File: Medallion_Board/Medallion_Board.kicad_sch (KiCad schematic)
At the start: 80 parts, among them IC1 Wio-SX1262, J1 SWD HEADER, J2 EXPANSION, P1 JST_BTN_1, P2 JST_BTN_2, P3 JST_BTN_3, Q1 DMG3415U, U1 MDBT50Q-1MV2, U2 MAX17048G_T10, U3 LC86LICMD, U4 RT9080-33GJ5, U5 MCP73831T-2ACI_OT, U6 BNO085, X1 USB4085-GF-A, Y1 32.768KHZ

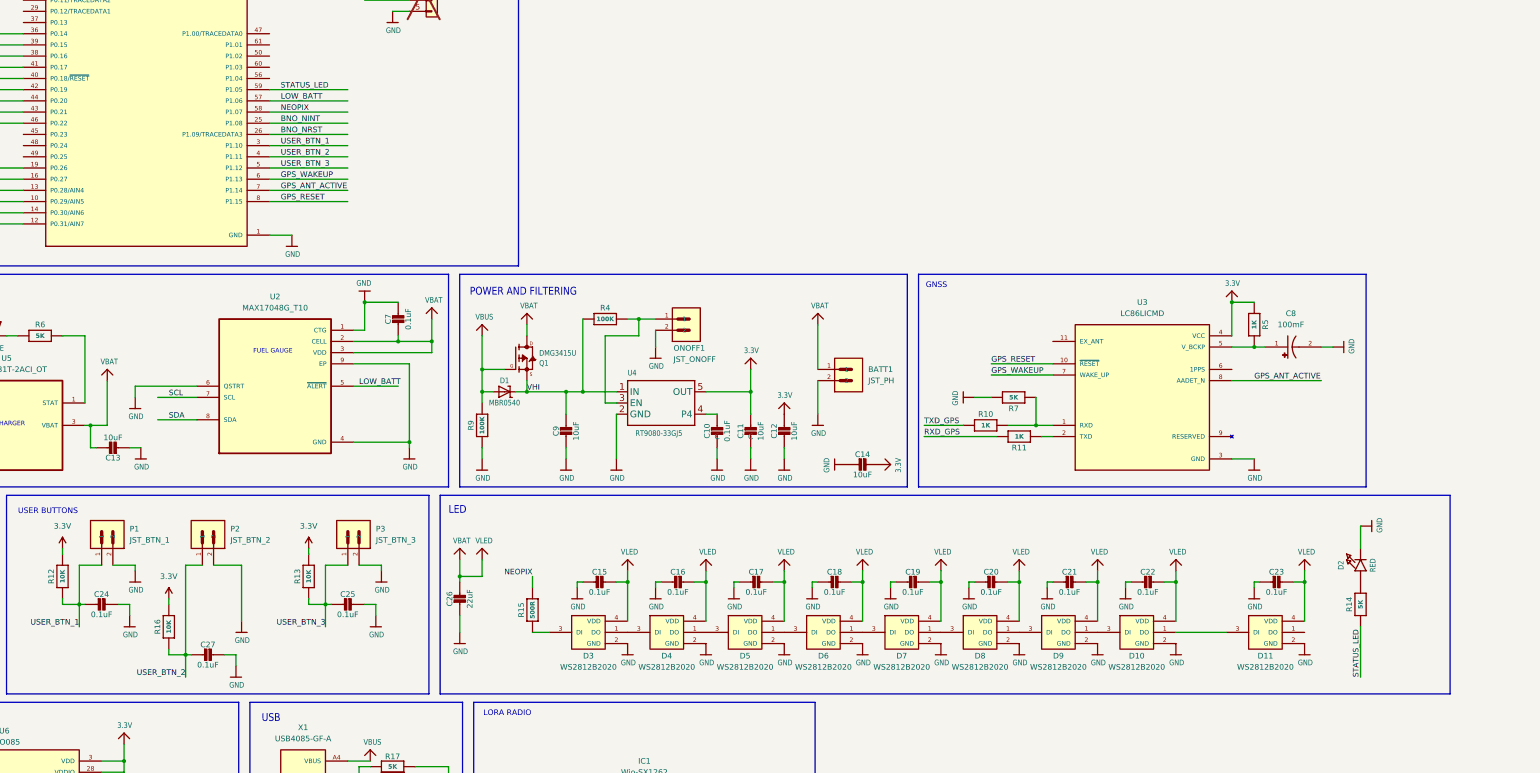
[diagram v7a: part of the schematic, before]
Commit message: Main board design is in place. Needs haptics and buzzer
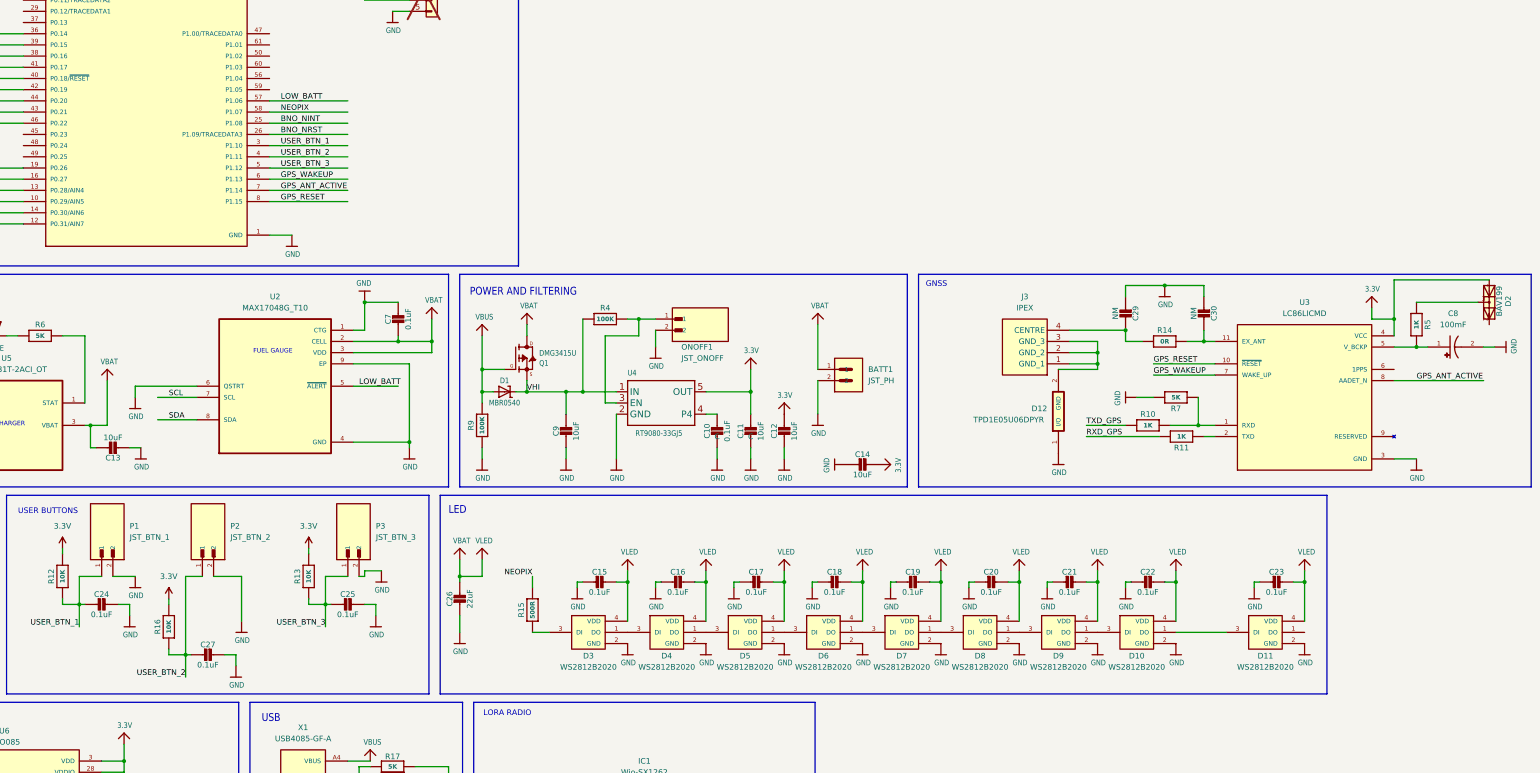
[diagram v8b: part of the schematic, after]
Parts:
- removed D2: RED, LED_SMD:LED_0603_1608Metric, symbol Adafruit ESP32-S3 8MB No PSRAM-eagle-import:LED0603_NOOUTLINE
- added C29, C30: NM, Capacitor_SMD:C_0402_1005Metric, symbol Adafruit ESP32-S3 8MB No PSRAM-eagle-import:CAP_CERAMIC0805-NOOUTLINE
- added D12: TPD1E05U06DPYR, TPD1E05U06DPYR:DIO_TPD1E05U06DPYR, symbol TPD1E05U06DPYR:TPD1E05U06DPYR
- added D2: BAV199, BAV199:SOT23, symbol BAV199:BAV199
- added J3: IPEX, RECE.20369:RECE20369001E01, symbol RECE_20369_001E_01:RECE.20369.001E.01
- ONOFF1, P1, P2, P3: footprint S2B-PH-SM4-TB_LF__SN_:JST_S2B-PH-SM4-TB_LF__SN_ -> SM02B-GHS-TB:JST_SM02B-GHS-TB; symbol S2B-PH-SM4-TB_LF__SN_:S2B-PH-SM4-TB_LF__SN_ -> SM02B-GHS-TB:SM02B-GHS-TB; DigiKey_Part_Number (none) -> 455-1564-1-ND; MP S2B-PH-SM4-TB (LF)(SN) -> SM02B-GHS-TB; MPN S2B-PH-SM4-TB(LF)(SN) -> SM02B-GHS-TB; PRICE 0.37 -> 0.26
- R14: value 5K -> 0R; footprint Resistor_SMD:R_0603_1608Metric -> Resistor_SMD:R_0402_1005Metric
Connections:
- net 3.3V: now also D2.1; no longer R5.1
- net GND: now also C29.2, C30.2, D12.1 (I/O)
- net at R14.2: now also U3.11 (EX_ANT), C30.1
- net STATUS_LED: no longer names the net of U1.59 (P1.05)
- net STATUS_LED: no longer R14.1
- new net: D12.2 (GND), J3.1 (GND_1), J3.2 (GND_2), J3.3 (GND_3)
- new net: D2.3, R5.1
- new net: C29.1, J3.4 (CENTRE), R14.1
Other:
- moved on the sheet: C8, R10, R11, R5, R7, U3
